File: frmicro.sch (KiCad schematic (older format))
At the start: 22 parts, among them P1 USB_C_Plug_USB2.0, P2 USB_C_Plug, SW1 SW_Push, U1 ATmega32U4-AU, Y1 16Mhz

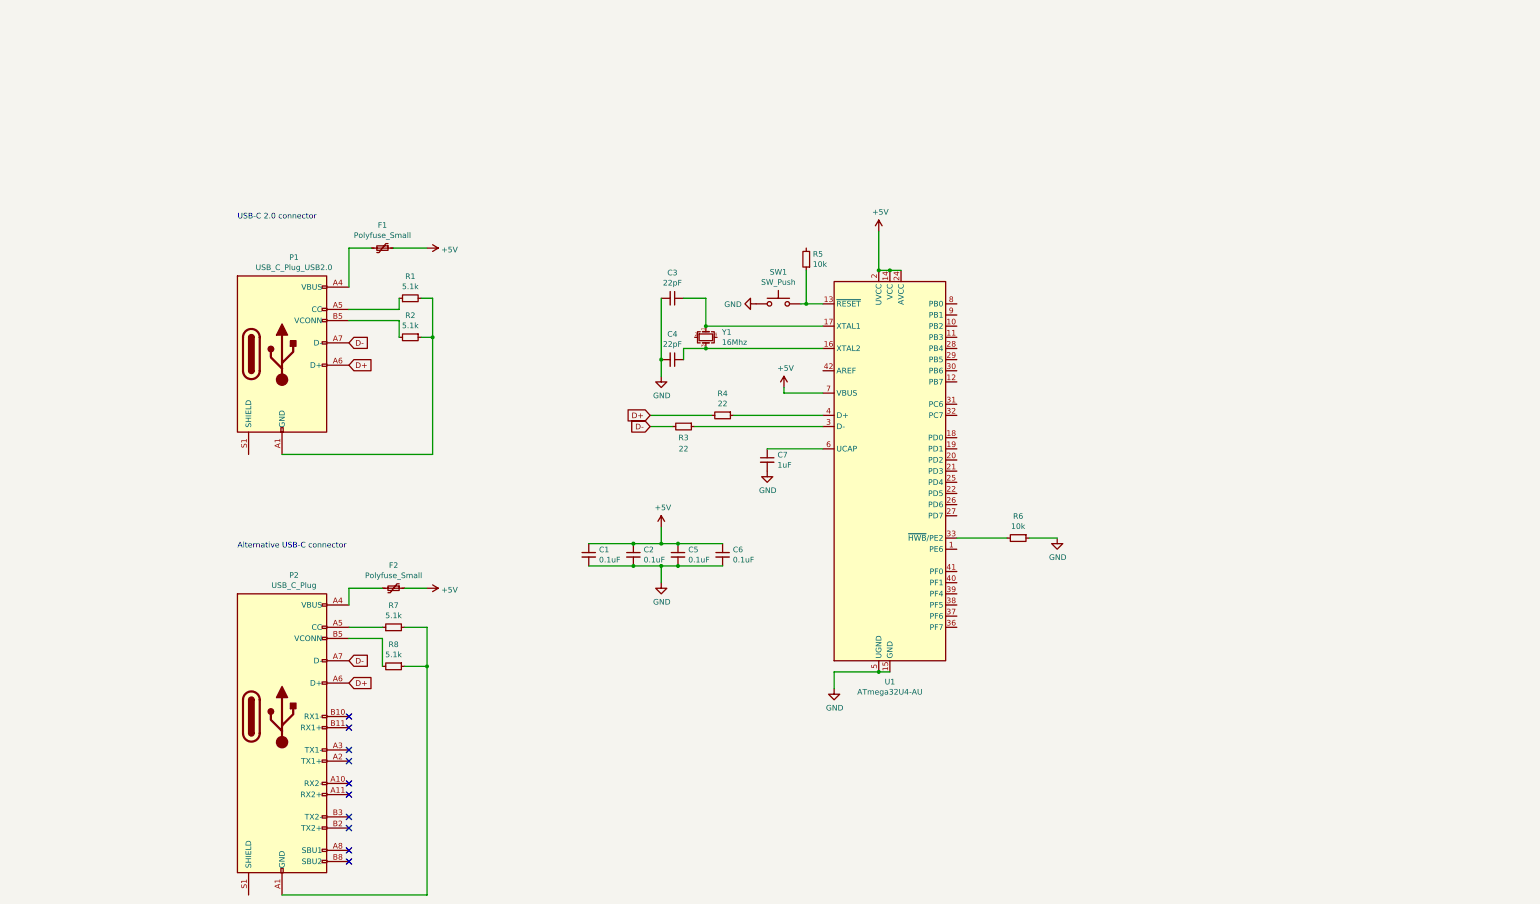
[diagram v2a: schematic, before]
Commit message: change usb c connector and add connectors
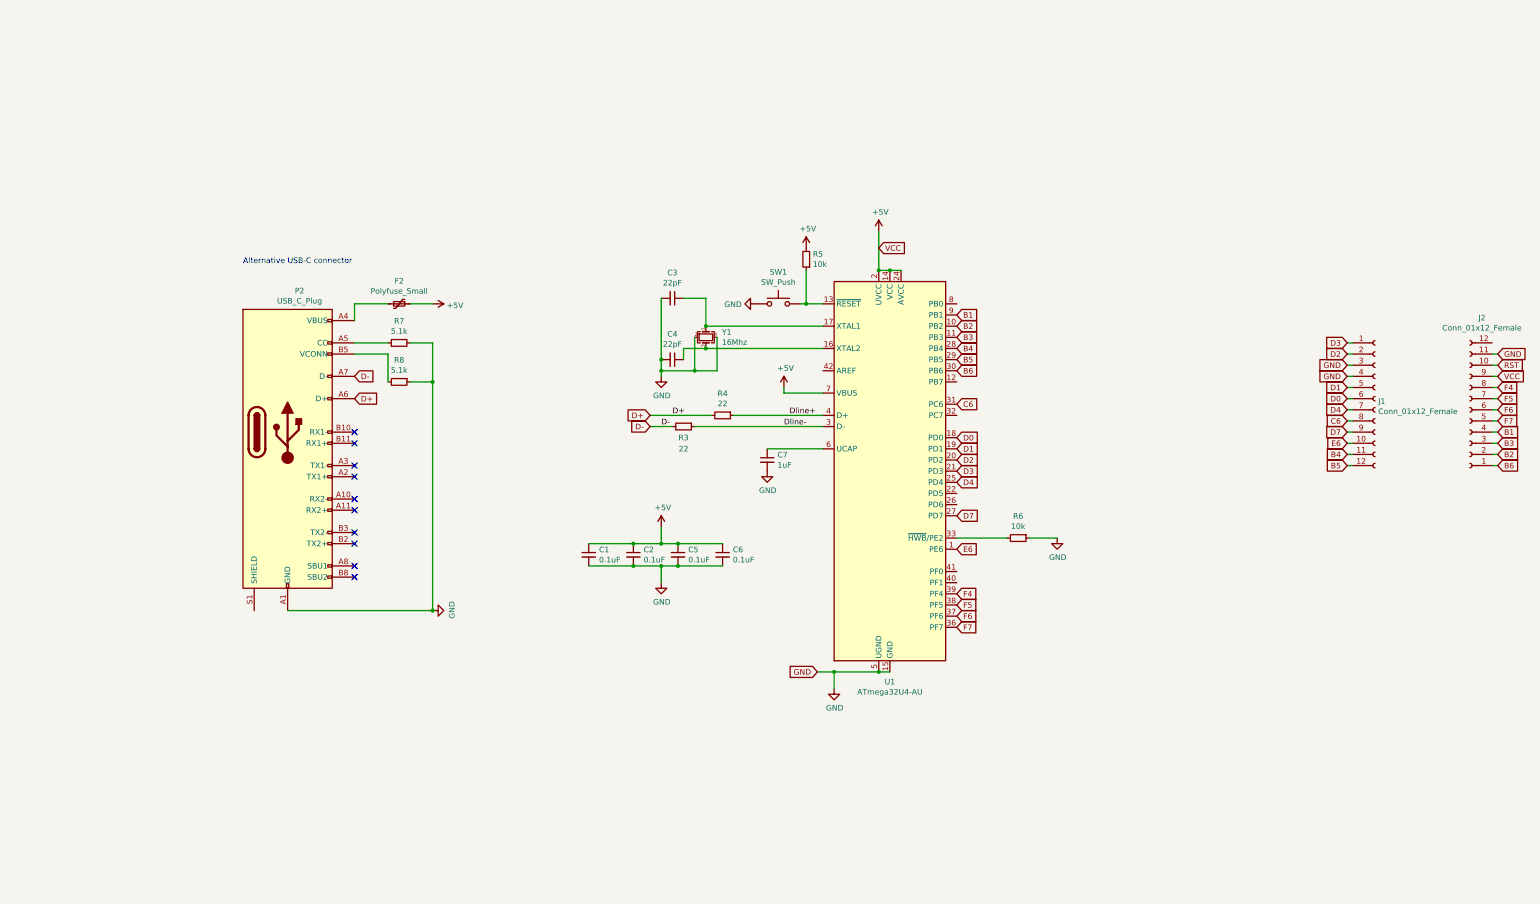
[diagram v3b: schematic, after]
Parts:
- removed F1: Polyfuse_Small, Fuse:Fuse_0805_2012Metric, symbol Device:Polyfuse_Small
- removed P1: USB_C_Plug_USB2.0, Connector_USB:USB_C_Plug_JAE_DX07P024AJ1, symbol Connector:USB_C_Plug_USB2.0
- removed R1, R2: 5.1k, Resistor_SMD:R_0805_2012Metric, symbol Device:R_Small
- added J1, J2: Conn_01x12_Female, Connector_PinHeader_2.54mm:PinHeader_1x12_P2.54mm_Vertical, symbol Connector:Conn_01x12_Female
- P2: footprint Connector_USB:USB_C_Plug_JAE_DX07P024AJ1 -> misc:GCT_USB4155-03-C_REVA
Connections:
- net +5V: now also R5.2, J2.9 (Pin_9)
- net GND: now also P2.A1 (GND), P2.A12 (GND), P2.B1 (GND), P2.B12 (GND), R7.2, R8.1, Y1.2, Y1.4, J1.3 (Pin_3), J1.4 (Pin_4), J2.11 (Pin_11)
- net E6: now reaches U1.1 (PE6)
- net E6: now also J1.10 (Pin_10)
- net B2: now reaches U1.10 (PB2)
- net B2: now also J2.2 (Pin_2)
- net B3: now reaches U1.11 (PB3)
- net B3: now also J2.3 (Pin_3)
- net D0: now reaches U1.18 (PD0)
- net D0: now also J1.6 (Pin_6)
- net D1: now reaches U1.19 (PD1)
- net D1: now also J1.5 (Pin_5)
- net D2: now reaches U1.20 (PD2)
- net D2: now also J1.2 (Pin_2)
- net D3: now reaches U1.21 (PD3)
- net D3: now also J1.1 (Pin_1)
- net D4: now reaches U1.25 (PD4)
- net D4: now also J1.7 (Pin_7)
- net D7: now reaches U1.27 (PD7)
- net D7: now also J1.9 (Pin_9)
- net B4: now reaches U1.28 (PB4)
- net B4: now also J1.11 (Pin_11)
- net B5: now reaches U1.29 (PB5)
- net B5: now also J1.12 (Pin_12)
- net Dline-: now reaches R3.1, U1.3 (D-)
- net B6: now reaches U1.30 (PB6)
- net B6: now also J2.1 (Pin_1)
- net C6: now reaches U1.31 (PC6)
- net C6: now also J1.8 (Pin_8)
- net F7: now reaches U1.36 (PF7)
- net F7: now also J2.5 (Pin_5)
- net F6: now reaches U1.37 (PF6)
- net F6: now also J2.6 (Pin_6)
- net F5: now reaches U1.38 (PF5)
- net F5: now also J2.7 (Pin_7)
- net F4: now reaches U1.39 (PF4)
- net F4: now also J2.8 (Pin_8)
- net Dline+: now reaches R4.1, U1.4 (D+)
- net B1: now reaches U1.9 (PB1)
- net B1: now also J2.4 (Pin_4)
- new net RST: J2.10 (Pin_10)
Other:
- note removed: "USB-C 2.0 connector"
- moved on the sheet: F2, P2, R7, R8

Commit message: add pro micro schematics and work from that.
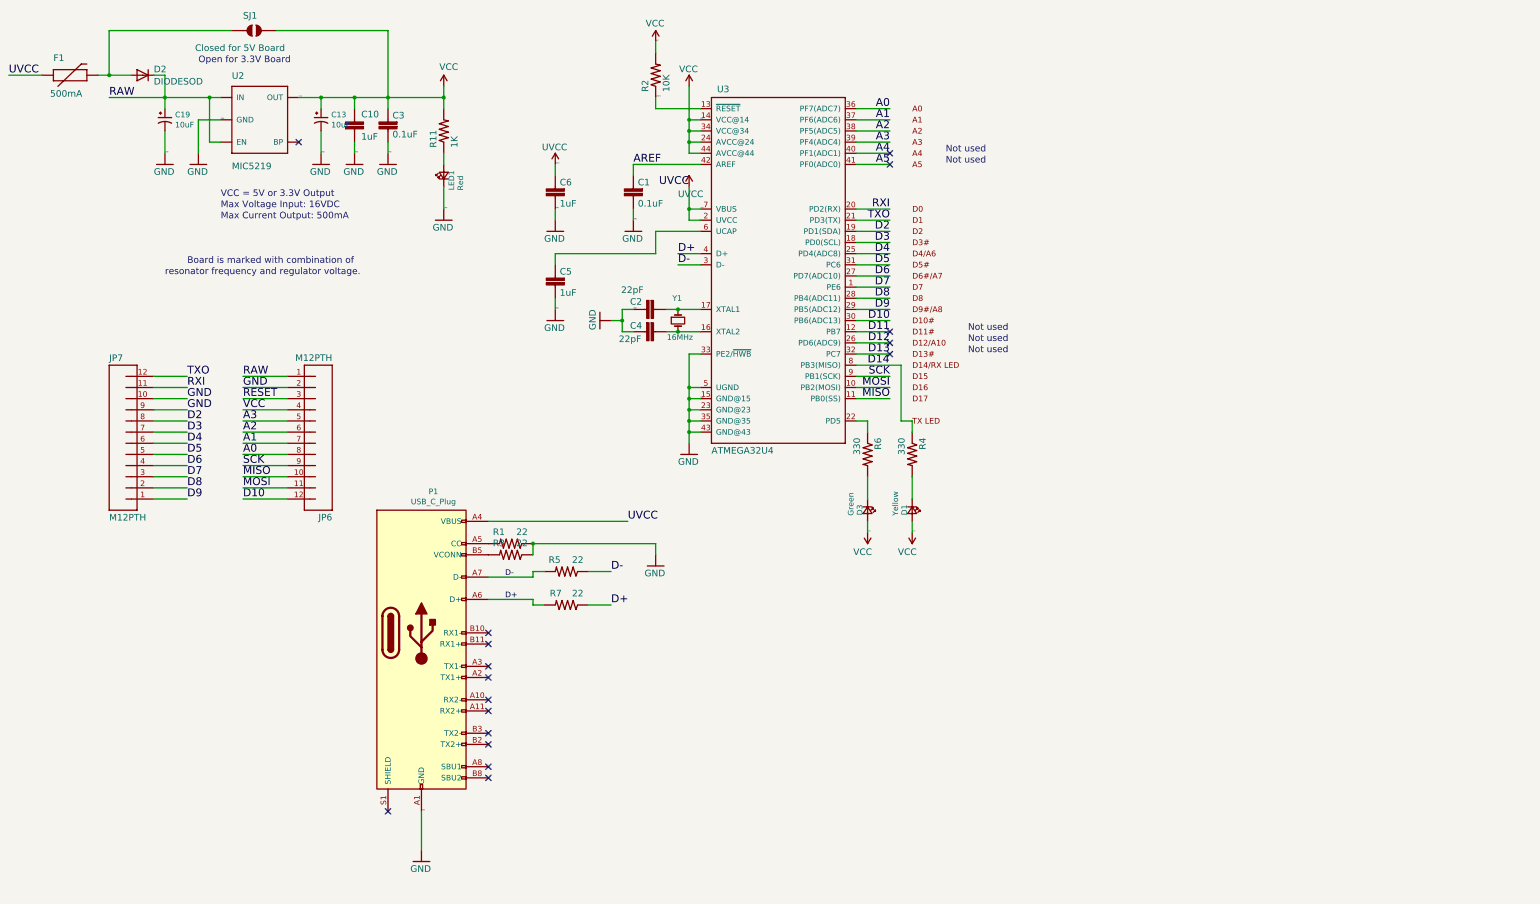
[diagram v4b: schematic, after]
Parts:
- removed C1, C2, C5, C6: 0.1uF, Capacitor_SMD:C_0805_2012Metric, symbol Device:C_Small
- removed C3, C4: 22pF, Capacitor_SMD:C_0805_2012Metric, symbol Device:C_Small
- removed C7: 1uF, Capacitor_SMD:C_0805_2012Metric, symbol Device:C_Small
- removed F2: Polyfuse_Small, Fuse:Fuse_0805_2012Metric, symbol Device:Polyfuse_Small
- removed J1, J2: Conn_01x12_Female, Connector_PinHeader_2.54mm:PinHeader_1x12_P2.54mm_Vertical, symbol Connector:Conn_01x12_Female
- removed P2: USB_C_Plug, misc:GCT_USB4155-03-C_REVA, symbol Connector:USB_C_Plug
- removed R3, R4: 22, Resistor_SMD:R_0805_2012Metric, symbol Device:R_Small
- removed R5, R6: 10k, Resistor_SMD:R_0805_2012Metric, symbol Device:R_Small
- removed R7, R8: 5.1k, Resistor_SMD:R_0805_2012Metric, symbol Device:R_Small
- removed SW1: SW_Push, misc:SW_PTS636_SM43J_SMTR_LFS, symbol Switch:SW_Push
- removed U1: ATmega32U4-AU, Package_QFP:TQFP-44_10x10mm_P0.8mm, symbol MCU_Microchip_ATmega:ATmega32U4-AU
- removed Y1: 16Mhz, Crystal:Crystal_SMD_3225-4Pin_3.2x2.5mm, symbol Device:Crystal_GND24_Small
- added C1, C3: 0.1uF, Capacitor_SMD:C_0603_1608Metric, symbol frmicro-eagle-import:CAP0603-CAP
- added C10, C5, C6: 1uF, Capacitor_SMD:C_0603_1608Metric, symbol frmicro-eagle-import:CAP0603-CAP
- added C13, C19: 10uF, Capacitor_Tantalum_SMD:CP_EIA-3216-18_Kemet-A, symbol Device:CP1_Small
- added C2, C4: 22pF, Capacitor_SMD:C_0603_1608Metric, symbol frmicro-eagle-import:CAP0603-CAP
- added D1: Yellow, LED_SMD:LED_0603_1608Metric, symbol Device:LED_Small
- added D2: DIODESOD, Diode_SMD:D_SOD-323, symbol frmicro-eagle-import:DIODESOD
- added D3: Green, LED_SMD:LED_0603_1608Metric, symbol Device:LED_Small
- added F1: 500mA, Fuse:Fuse_1206_3216Metric, symbol frmicro-eagle-import:PTCSMD
- added JP6, JP7: M12PTH, Connector_PinSocket_2.54mm:PinSocket_1x12_P2.54mm_Vertical, symbol frmicro-eagle-import:M12PTH
- added LED1: Red, LED_SMD:LED_0603_1608Metric, symbol Device:LED_Small
- added P1: USB_C_Plug, misc:GCT_USB4155-03-C_REVA, symbol Connector:USB_C_Plug
- added R1, R3, R5, R7: 22, Resistor_SMD:R_0603_1608Metric, symbol frmicro-eagle-import:RESISTOR0603-RES
- added R11: 1K, Resistor_SMD:R_0603_1608Metric, symbol frmicro-eagle-import:RESISTOR0603-RES
- added R2: 10K, Resistor_SMD:R_0603_1608Metric, symbol frmicro-eagle-import:RESISTOR0603-RES
- added R4, R6: 330, Resistor_SMD:R_0603_1608Metric, symbol frmicro-eagle-import:RESISTOR0603-RES
- added SJ1: Closed for 5V Board, Jumper:SolderJumper-2_P1.3mm_Open_Pad1.0x1.5mm, symbol frmicro-eagle-import:SOLDERJUMPERNC
- added U2: MIC5219, Package_TO_SOT_SMD:SOT-23-5, symbol frmicro-eagle-import:V_REG_LDOSMD
- added U3: ATMEGA32U4, misc:QFN-44-1EP_7x7mm_Pitch0.5mm, symbol frmicro-eagle-import:ATMEGA32U4OUTFAKES
- added Y1: 16MHz, Crystal:Crystal_SMD_5032-2Pin_5.0x3.2mm, symbol Device:Crystal_Small
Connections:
- net D+: now also P1.A6 (D+), R7.1, R7.2, U3.4 (D+)
- net D-: now also P1.A7 (D-), R5.1, R5.2, U3.3 (D-)
- net D2: now also JP7.8, U3.19 (PD1(SDA))
- net D3: now also JP7.7, U3.18 (PD0(SCL))
- net D4: now also JP7.6, U3.25 (PD4(ADC8))
- net D7: now also JP7.3, U3.1 (PE6)
- net GND: now also C1.1, C10.2, C13.2, C19.2, C2.2, C3.1, C4.2, C5.1, C6.1, JP6.2, JP7.10, JP7.9, LED1.1 (K), P1.A1 (GND), P1.A12 (GND), P1.B1 (GND), P1.B12 (GND), U2.2 (GND), U3.15 (GND@15), U3.23 (GND@23), U3.33 (PE2/~HWB), U3.35 (GND@35), U3.43 (GND@43), U3.5 (UGND)
- new net: D2.2 (A), F1.2, SJ1.1
- new net: P1.A5 (CC), R1.2
- new net: P1.B5 (VCONN), R3.2
- new net: R1.1, R3.1
- new net: C2.1, U3.17 (XTAL1), Y1.1
- new net: C4.1, U3.16 (XTAL2), Y1.2
- new net: LED1.2 (A), R11.1
- new net: D3.1 (K), R6.2
- new net: D1.1 (K), R4.2
- new net: C5.2, U3.6 (UCAP)
- new net: R6.1, U3.22 (PD5)
- new net A0: JP6.8, U3.36 (PF7(ADC7))
- new net A1: JP6.7, U3.37 (PF6(ADC6))
- new net A2: JP6.6, U3.38 (PF5(ADC5))
- new net A3: JP6.5, U3.39 (PF4(ADC4))
- new net A4: U3.40 (PF1(ADC1))
- new net A5: U3.41 (PF0(ADC0))
- new net AREF: C1.2, U3.42 (AREF)
- new net D10: JP6.12, U3.30 (PB6(ADC13))
- new net D11: U3.12 (PB7)
- new net D12: U3.26 (PD6(ADC9))
- new net D13: U3.32 (PC7)
- new net D14: R4.1, U3.8 (PB3(MISO))
- new net D5: JP7.5, U3.31 (PC6)
- new net D6: JP7.4, U3.27 (PD7(ADC10))
- new net D8: JP7.2, U3.28 (PB4(ADC11))
- new net D9: JP7.1, U3.29 (PB5(ADC12))
- new net MISO: JP6.10, U3.11 (PB0(SS))
- new net MOSI: JP6.11, U3.10 (PB2(MOSI))
- new net RAW: C19.1, D2.1 (C), JP6.1, U2.1 (IN), U2.3 (EN)
- new net RESET: JP6.3, R2.1, U3.13 (~RESET)
- new net RXI: JP7.11, U3.20 (PD2(RX))
- new net SCK: JP6.9, U3.9 (PB1(SCK))
- new net TXO: JP7.12, U3.21 (PD3(TX))
- new net UVCC: C6.2, F1.1, P1.A4 (VBUS), P1.A9 (VBUS), P1.B4 (VBUS), P1.B9 (VBUS), U3.2 (UVCC), U3.7 (VBUS)
- new net VCC: C10.1, C13.1, C3.2, D1.2 (A), D3.2 (A), JP6.4, R11.2, R2.2, SJ1.2, U2.5 (OUT), U3.14 (VCC@14), U3.24 (AVCC@24), U3.34 (VCC@34), U3.44 (AVCC@44)
- no-connect marks 10 -> 17
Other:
- note added: "Board is marked with combination of"
- note added: "Max Current Output: 500mA"
- note added: "Max Voltage Input: 16VDC"
- note added: "Not used"
- note added: "Open for 3.3V Board"
- note added: "VCC = 5V or 3.3V Output"
- note added: "resonator frequency and regulator voltage."
- note removed: "Alternative USB-C connector"
